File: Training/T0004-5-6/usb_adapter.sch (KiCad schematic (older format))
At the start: 23 parts, among them J1 modular8_rev3_comms_out, P1 USB_OTG, U1 FT231X, U2 TE_1825058-1

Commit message: fixed training schematic
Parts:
- U2: symbol TE_1825058-1 -> TE_1825058-1-RESCUE-usb_adapter
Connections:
- net +5V: now also L1.1
- net POWER_OUT: now also U2.2; no longer U2.4
- net PROGRAM: now also U2.2; no longer U2.3
- net at J1.7 (~SS/PGM): now also U2.1; no longer U2.2
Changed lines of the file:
@@
 EESchema Schematic File Version 2
+LIBS:usb_adapter-rescue
 LIBS:power
 LIBS:device
@@
 LIBS:contrib
 LIBS:valves
-LIBS:ft231x
 LIBS:open_robotics
 LIBS:usb_adapter-cache
@@
 L +5V #PWR2
 U 1 1 5622C0D5
-P 2550 2500
-F 0 "#PWR2" H 2550 2350 50  0001 C CNN
-F 1 "+5V" H 2550 2640 50  0000 C CNN
-F 2 "" H 2550 2500 60  0000 C CNN
-F 3 "" H 2550 2500 60  0000 C CNN
-	1    2550 2500
+P 2100 2600
+F 0 "#PWR2" H 2100 2450 50  0001 C CNN
+F 1 "+5V" H 2100 2740 50  0000 C CNN
+F 2 "" H 2100 2600 60  0000 C CNN
+F 3 "" H 2100 2600 60  0000 C CNN
+	1    2100 2600
 	1    0    0    -1
 $EndComp
@@
 $EndComp
 $Comp
-L TE_1825058-1 U2
+L TE_1825058-1-RESCUE-usb_adapter U2
 U 1 1 5629AB3C
 P 6900 2400
@@
 $EndComp
 $Comp
-L TE_1825058-1 U2
+L TE_1825058-1-RESCUE-usb_adapter U2
 U 2 1 5629ABC7
 P 9100 3550
@@
 $EndComp
 Wire Wire Line
-	3350 3250 3350 3350
-Wire Wire Line
-	3350 3350 3350 3800
+	3350 3250 3350 3800
 Wire Wire Line
 	3350 3350 3450 3350
 Wire Wire Line
-	1850 3800 1850 4200
-Wire Wire Line
-	1850 4200 1850 4350
+	1850 3800 1850 4350
 Wire Wire Line
 	1850 3800 1550 3800
@@
 	4000 4700 4000 4750
 Wire Wire Line
-	4000 4750 4050 4750
-Wire Wire Line
-	4050 4750 4100 4750
+	4000 4750 4100 4750
 Wire Wire Line
 	4100 4750 4100 4700
@@
 Connection ~ 4050 4750
 Wire Wire Line
-	1550 3500 2450 3500
-Wire Wire Line
-	2450 3500 2500 3500
+	1550 3500 2500 3500
 Wire Wire Line
 	2800 3500 3450 3500
@@
 	3450 3600 3150 3600
 Wire Wire Line
-	1550 3600 2800 3600
-Wire Wire Line
-	2800 3600 2850 3600
+	1550 3600 2850 3600
 Wire Wire Line
 	3350 3800 3450 3800
@@
 	2800 4200 2800 4100
 Wire Wire Line
-	1850 4200 2100 4200
-Wire Wire Line
-	2100 4200 2450 4200
-Wire Wire Line
-	2450 4200 2800 4200
+	1850 4200 2800 4200
 Connection ~ 1850 4200
 Wire Wire Line
@@
 	3450 1700 3450 1800
 Wire Wire Line
-	3100 1800 3450 1800
-Wire Wire Line
-	3450 1800 3650 1800
-Wire Wire Line
-	3650 1800 3850 1800
+	3100 1800 3850 1800
 Wire Wire Line
 	3850 1800 3850 1700
@@
 	5200 2000 5200 1850
 Wire Wire Line
-	5200 1850 5500 1850
-Wire Wire Line
-	5500 1850 5800 1850
-Wire Wire Line
-	5800 1850 6100 1850
+	5200 1850 6100 1850
 Wire Wire Line
 	5800 1850 5800 2000
 Wire Wire Line
-	5500 1700 5500 1850
-Wire Wire Line
-	5500 1850 5500 2000
+	5500 1700 5500 2000
 Connection ~ 5500 1850
 Wire Wire Line
@@
 	5200 2800 5200 2900
 Wire Wire Line
-	2100 3250 2100 3400
-Wire Wire Line
-	2100 3400 2100 3800
+	2100 3250 2100 3800
 Connection ~ 2100 3400
 Wire Wire Line
@@
 	3100 1400 3100 1300
 Wire Wire Line
-	3100 1300 3300 1300
-Wire Wire Line
-	3300 1300 3450 1300
+	3100 1300 3450 1300
 Wire Wire Line
 	3450 1300 3450 1400
@@
 	4800 4000 9250 4000
 Wire Wire Line
-	6900 2700 6900 2850
-Wire Wire Line
-	6900 2850 6900 3750
+	6900 2700 6900 3750
 Wire Wire Line
 	8600 2850 6900 2850
@@
 	9700 3000 9700 3100
 Wire Wire Line
-	9700 3400 9700 3550
-Wire Wire Line
-	9700 3550 9700 4000
+	9700 3400 9700 4000
 Wire Wire Line
 	9700 4000 9550 4000
@@
 Text Notes 7450 3950 0    60   ~ 0
 Standardized header
-Text Notes 6100 1850 0    60   ~ 0
+Text Notes 5950 1850 0    60   ~ 0
 Ensures that\ndevice is on
 $EndSCHEMATC

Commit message: ready for design to be checked
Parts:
- J1: footprint (none) -> open_robotics:modular8_rev3_edge
- U2: footprint (none) -> open_robotics:DIPSWITCH_SMT_ALCO_2CCT
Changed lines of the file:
@@
 LIBS:contrib
 LIBS:valves
-LIBS:open_robotics
 LIBS:usb_adapter-cache
 EELAYER 25 0
@@
 $EndComp
 $Comp
-L GND #PWR1
+L GND #PWR01
 U 1 1 5622C099
 P 1850 4350
-F 0 "#PWR1" H 1850 4100 50  0001 C CNN
+F 0 "#PWR01" H 1850 4100 50  0001 C CNN
 F 1 "GND" H 1850 4200 50  0000 C CNN
 F 2 "" H 1850 4350 60  0000 C CNN
@@
 $EndComp
 $Comp
-L +5V #PWR2
+L +5V #PWR02
 U 1 1 5622C0D5
 P 2100 2600
-F 0 "#PWR2" H 2100 2450 50  0001 C CNN
+F 0 "#PWR02" H 2100 2450 50  0001 C CNN
 F 1 "+5V" H 2100 2740 50  0000 C CNN
 F 2 "" H 2100 2600 60  0000 C CNN
@@
 $EndComp
 $Comp
-L +3V3 #PWR5
+L +3V3 #PWR03
 U 1 1 5622C14E
 P 3350 3250
-F 0 "#PWR5" H 3350 3100 50  0001 C CNN
+F 0 "#PWR03" H 3350 3100 50  0001 C CNN
 F 1 "+3V3" H 3350 3390 50  0000 C CNN
 F 2 "" H 3350 3250 60  0000 C CNN
@@
 $EndComp
 $Comp
-L GND #PWR7
+L GND #PWR04
 U 1 1 5622DDA1
 P 4050 4850
-F 0 "#PWR7" H 4050 4600 50  0001 C CNN
+F 0 "#PWR04" H 4050 4600 50  0001 C CNN
 F 1 "GND" H 4050 4700 50  0000 C CNN
 F 2 "" H 4050 4850 60  0000 C CNN
@@
 $EndComp
 $Comp
-L +5V #PWR8
+L +5V #PWR05
 U 1 1 5622EF00
 P 4100 2950
-F 0 "#PWR8" H 4100 2800 50  0001 C CNN
+F 0 "#PWR05" H 4100 2800 50  0001 C CNN
 F 1 "+5V" H 4100 3090 50  0000 C CNN
 F 2 "" H 4100 2950 60  0000 C CNN
@@
 $EndComp
 $Comp
-L +3V3 #PWR9
+L +3V3 #PWR06
 U 1 1 5622F2DF
 P 4300 2950
-F 0 "#PWR9" H 4300 2800 50  0001 C CNN
+F 0 "#PWR06" H 4300 2800 50  0001 C CNN
 F 1 "+3V3" H 4300 3090 50  0000 C CNN
 F 2 "" H 4300 2950 60  0000 C CNN
@@
 ~SLEEP
 $Comp
-L +5V #PWR3
+L +5V #PWR07
 U 1 1 562300CF
 P 3300 1200
-F 0 "#PWR3" H 3300 1050 50  0001 C CNN
+F 0 "#PWR07" H 3300 1050 50  0001 C CNN
 F 1 "+5V" H 3300 1340 50  0000 C CNN
 F 2 "" H 3300 1200 60  0000 C CNN
@@
 $EndComp
 $Comp
-L +3V3 #PWR6
+L +3V3 #PWR08
 U 1 1 562301B6
 P 3850 1200
-F 0 "#PWR6" H 3850 1050 50  0001 C CNN
+F 0 "#PWR08" H 3850 1050 50  0001 C CNN
 F 1 "+3V3" H 3850 1340 50  0000 C CNN
 F 2 "" H 3850 1200 60  0000 C CNN
@@
 $EndComp
 $Comp
-L GND #PWR4
+L GND #PWR09
 U 1 1 56230399
 P 3650 1900
-F 0 "#PWR4" H 3650 1650 50  0001 C CNN
+F 0 "#PWR09" H 3650 1650 50  0001 C CNN
 F 1 "GND" H 3650 1750 50  0000 C CNN
 F 2 "" H 3650 1900 60  0000 C CNN
@@
 $EndComp
 $Comp
-L GND #PWR10
+L GND #PWR010
 U 1 1 56231F36
 P 5200 2900
-F 0 "#PWR10" H 5200 2650 50  0001 C CNN
+F 0 "#PWR010" H 5200 2650 50  0001 C CNN
 F 1 "GND" H 5200 2750 50  0000 C CNN
 F 2 "" H 5200 2900 60  0000 C CNN
@@
 $EndComp
 $Comp
-L +3V3 #PWR11
+L +3V3 #PWR011
 U 1 1 562364F3
 P 5500 1700
-F 0 "#PWR11" H 5500 1550 50  0001 C CNN
+F 0 "#PWR011" H 5500 1550 50  0001 C CNN
 F 1 "+3V3" H 5500 1840 50  0000 C CNN
 F 2 "" H 5500 1700 60  0000 C CNN
@@
 F 0 "U2" V 6850 2650 60  0000 C CNN
 F 1 "TE_1825058-1" V 6950 2900 60  0000 C CNN
-F 2 "" H 7010 2400 60  0000 C CNN
+F 2 "open_robotics:DIPSWITCH_SMT_ALCO_2CCT" H 7010 2400 60  0001 C CNN
 F 3 "" H 7010 2400 60  0000 C CNN
 	1    6900 2400
@@
 F 0 "U2" H 8900 3800 60  0000 C CNN
 F 1 "TE_1825058-1" H 9150 3700 60  0000 C CNN
-F 2 "" H 9210 3550 60  0000 C CNN
+F 2 "open_robotics:DIPSWITCH_SMT_ALCO_2CCT" H 9210 3550 60  0001 C CNN
 F 3 "" H 9210 3550 60  0000 C CNN
 	2    9100 3550
@@
 F 0 "J1" H 8250 4000 60  0000 C CNN
 F 1 "modular8_rev3_comms_out" H 7950 3900 60  0000 C CNN
-F 2 "" H 7900 3500 60  0000 C CNN
+F 2 "open_robotics:modular8_rev3_edge" H 7900 3500 60  0001 C CNN
 F 3 "" H 7900 3500 60  0000 C CNN
 	1    7900 3500
@@
 $EndComp
 $Comp
-L +5V #PWR12
+L +5V #PWR012
 U 1 1 5629BADF
 P 6900 2000
-F 0 "#PWR12" H 6900 1850 50  0001 C CNN
+F 0 "#PWR012" H 6900 1850 50  0001 C CNN
 F 1 "+5V" H 6900 2140 50  0000 C CNN
 F 2 "" H 6900 2000 60  0000 C CNN
@@
 Capacitors, resistors and ferrite bead 0603 SMT packages\nLEDs 0805 package
 $Comp
-L GND #PWR?
+L GND #PWR013
 U 1 1 562A3E08
 P 7100 3550
-F 0 "#PWR?" H 7100 3300 50  0001 C CNN
+F 0 "#PWR013" H 7100 3300 50  0001 C CNN
 F 1 "GND" H 7100 3400 50  0000 C CNN
 F 2 "" H 7100 3550 60  0000 C CNN
@@
 	7100 3550 7300 3550
 $Comp
-L GND #PWR?
+L GND #PWR014
 U 1 1 562A3EDA
 P 8600 3650
-F 0 "#PWR?" H 8600 3400 50  0001 C CNN
+F 0 "#PWR014" H 8600 3400 50  0001 C CNN
 F 1 "GND" H 8600 3500 50  0000 C CNN
 F 2 "" H 8600 3650 60  0000 C CNN
@@
 	8600 3450 8600 3650
 $Comp
-L +3V3 #PWR?
+L +3V3 #PWR015
 U 1 1 562A597E
 P 9700 3000
-F 0 "#PWR?" H 9700 2850 50  0001 C CNN
+F 0 "#PWR015" H 9700 2850 50  0001 C CNN
 F 1 "+3V3" H 9700 3140 50  0000 C CNN
 F 2 "" H 9700 3000 60  0000 C CNN

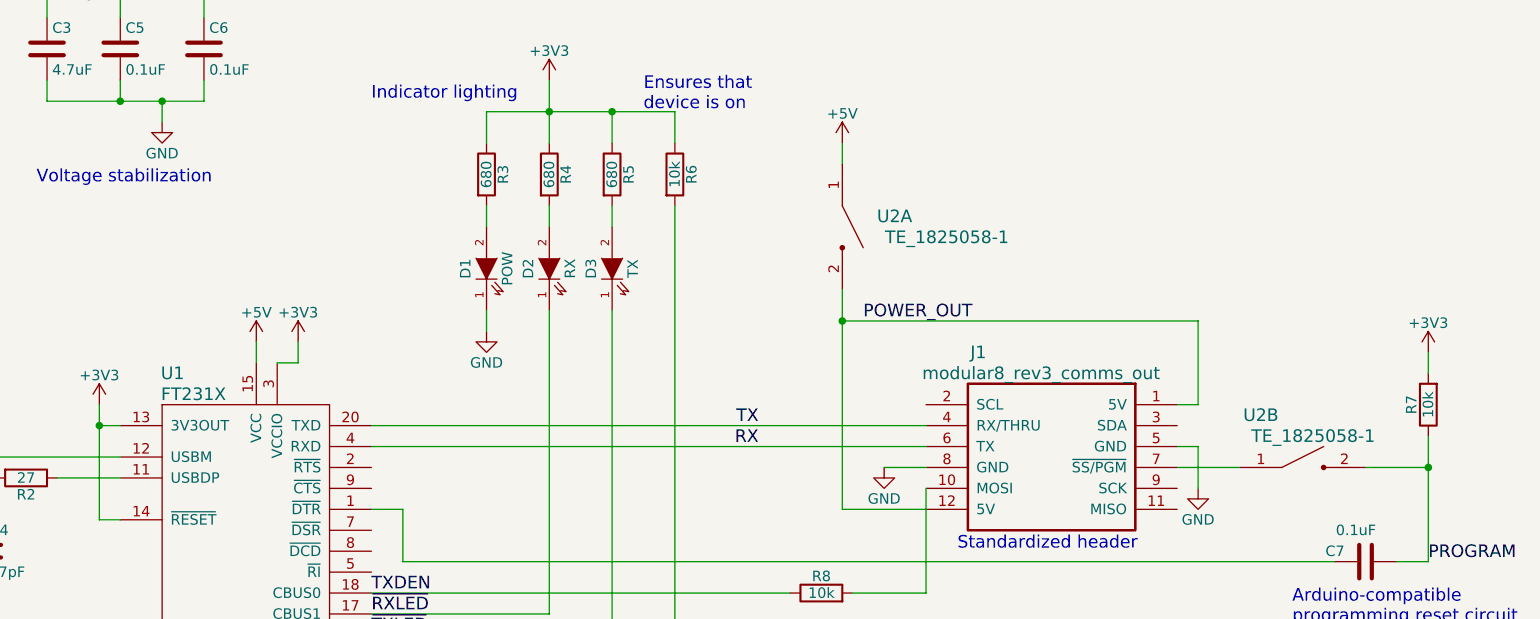
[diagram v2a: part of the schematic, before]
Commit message: fixed footprints, added suggestions
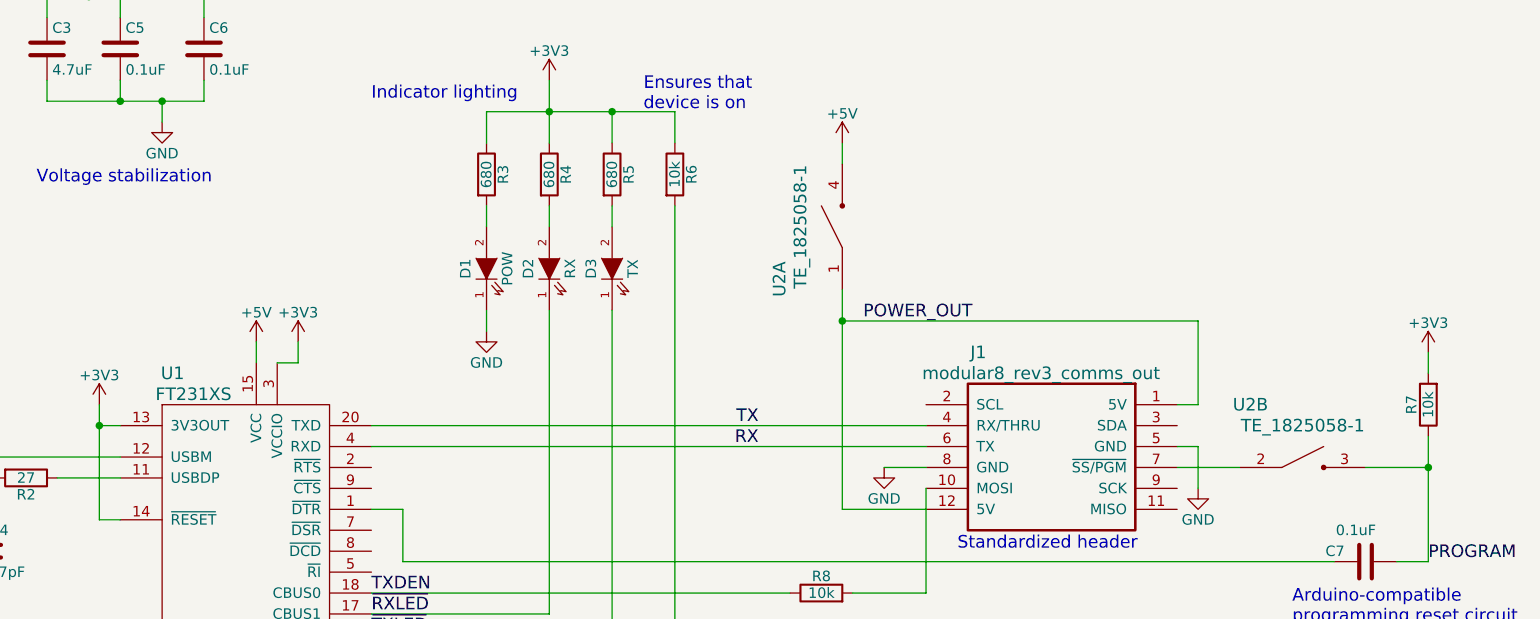
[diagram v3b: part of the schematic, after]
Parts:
- removed U1: FT231X, Housings_DFN_QFN:QFN-20-1EP_4x4mm_Pitch0.5mm, symbol FT231X
- removed U2: TE_1825058-1, open_robotics:DIPSWITCH_SMT_ALCO_2CCT, symbol TE_1825058-1-RESCUE-usb_adapter
- added U1: FT231XS, SMD_Packages:SSOP-20, symbol FT231XS
- added U2: TE_1825058-1, open_robotics:DIPSWITCH_SMT_ALCO_2CCT, symbol TE_1825058-1
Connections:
- net +3V3: now also U1.13 (3V3OUT), U1.14 (~RESET), U1.3 (VCCIO)
- net +5V: now also U1.15 (VCC), U2.4
- net GND: now also U1.16 (GND), U1.6 (GND)
- net POWER_OUT: now also U2.1
- net PROGRAM: now also U2.3
- net RX: now also U1.4 (RXD)
- net TX: now also U1.20 (TXD)
- net TXDEN: now also U1.18 (CBUS0)
- net ~RXLED: now also U1.17 (CBUS1)
- net ~SLEEP: now also U1.19 (CBUS3)
- net ~TXLED: now also U1.10 (CBUS2)
- net at C7.1: now also U1.1 (~DTR)
- net at R2.1: now also U1.11 (USBDP)
- net at R1.1: now also U1.12 (USBM)
- net at J1.7 (~SS/PGM): now also U2.2
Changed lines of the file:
@@
 LIBS:contrib
 LIBS:valves
+LIBS:open_robotics
 LIBS:usb_adapter-cache
 EELAYER 25 0
@@
 1
 $Comp
-L FT231X U1
-U 1 1 5622A3C5
-P 4050 3600
-F 0 "U1" H 3700 4100 60  0000 C CNN
-F 1 "FT231X" H 3800 4000 60  0000 C CNN
-F 2 "Housings_DFN_QFN:QFN-20-1EP_4x4mm_Pitch0.5mm" H 4000 4100 60  0001 C CNN
-F 3 "" H 4000 4100 60  0000 C CNN
-	1    4050 3600
-	1    0    0    -1
-$EndComp
-$Comp
 L R R2
 U 1 1 5622A6B9
@@
 F 3 "" H 5500 1700 60  0000 C CNN
 	1    5500 1700
-	1    0    0    -1
-$EndComp
-$Comp
-L TE_1825058-1-RESCUE-usb_adapter U2
-U 1 1 5629AB3C
-P 6900 2400
-F 0 "U2" V 6850 2650 60  0000 C CNN
-F 1 "TE_1825058-1" V 6950 2900 60  0000 C CNN
-F 2 "open_robotics:DIPSWITCH_SMT_ALCO_2CCT" H 7010 2400 60  0001 C CNN
-F 3 "" H 7010 2400 60  0000 C CNN
-	1    6900 2400
-	0    1    1    0
-$EndComp
-$Comp
-L TE_1825058-1-RESCUE-usb_adapter U2
-U 2 1 5629ABC7
-P 9100 3550
-F 0 "U2" H 8900 3800 60  0000 C CNN
-F 1 "TE_1825058-1" H 9150 3700 60  0000 C CNN
-F 2 "open_robotics:DIPSWITCH_SMT_ALCO_2CCT" H 9210 3550 60  0001 C CNN
-F 3 "" H 9210 3550 60  0000 C CNN
-	2    9100 3550
 	1    0    0    -1
 $EndComp
@@
 Text Notes 5950 1850 0    60   ~ 0
 Ensures that\ndevice is on
+$Comp
+L TE_1825058-1 U2
+U 1 1 563E9D2D
+P 6900 2400
+F 0 "U2" H 6650 2700 60  0000 C CNN
+F 1 "TE_1825058-1" H 6900 2600 60  0000 C CNN
+F 2 "open_robotics:DIPSWITCH_SMT_ALCO_2CCT" H 7010 2400 60  0001 C CNN
+F 3 "" H 7010 2400 60  0000 C CNN
+	1    6900 2400
+	0    -1   -1   0
+$EndComp
+$Comp
+L TE_1825058-1 U2
+U 2 1 563E9E4A
+P 9100 3550
+F 0 "U2" H 8850 3850 60  0000 C CNN
+F 1 "TE_1825058-1" H 9100 3750 60  0000 C CNN
+F 2 "open_robotics:DIPSWITCH_SMT_ALCO_2CCT" H 9210 3550 60  0001 C CNN
+F 3 "" H 9210 3550 60  0000 C CNN
+	2    9100 3550
+	1    0    0    -1
+$EndComp
+$Comp
+L FT231XS U1
+U 1 1 563E9F58
+P 4050 3600
+F 0 "U1" H 3700 4100 60  0000 C CNN
+F 1 "FT231XS" H 3800 4000 60  0000 C CNN
+F 2 "SMD_Packages:SSOP-20" H 4000 4100 60  0001 C CNN
+F 3 "" H 4000 4100 60  0000 C CNN
+	1    4050 3600
+	1    0    0    -1
+$EndComp
 $EndSCHEMATC
